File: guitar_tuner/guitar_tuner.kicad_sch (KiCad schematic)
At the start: 8 parts, among them SW1 Reset, SW2 Boot, U1 ESP32-S2-SOLO

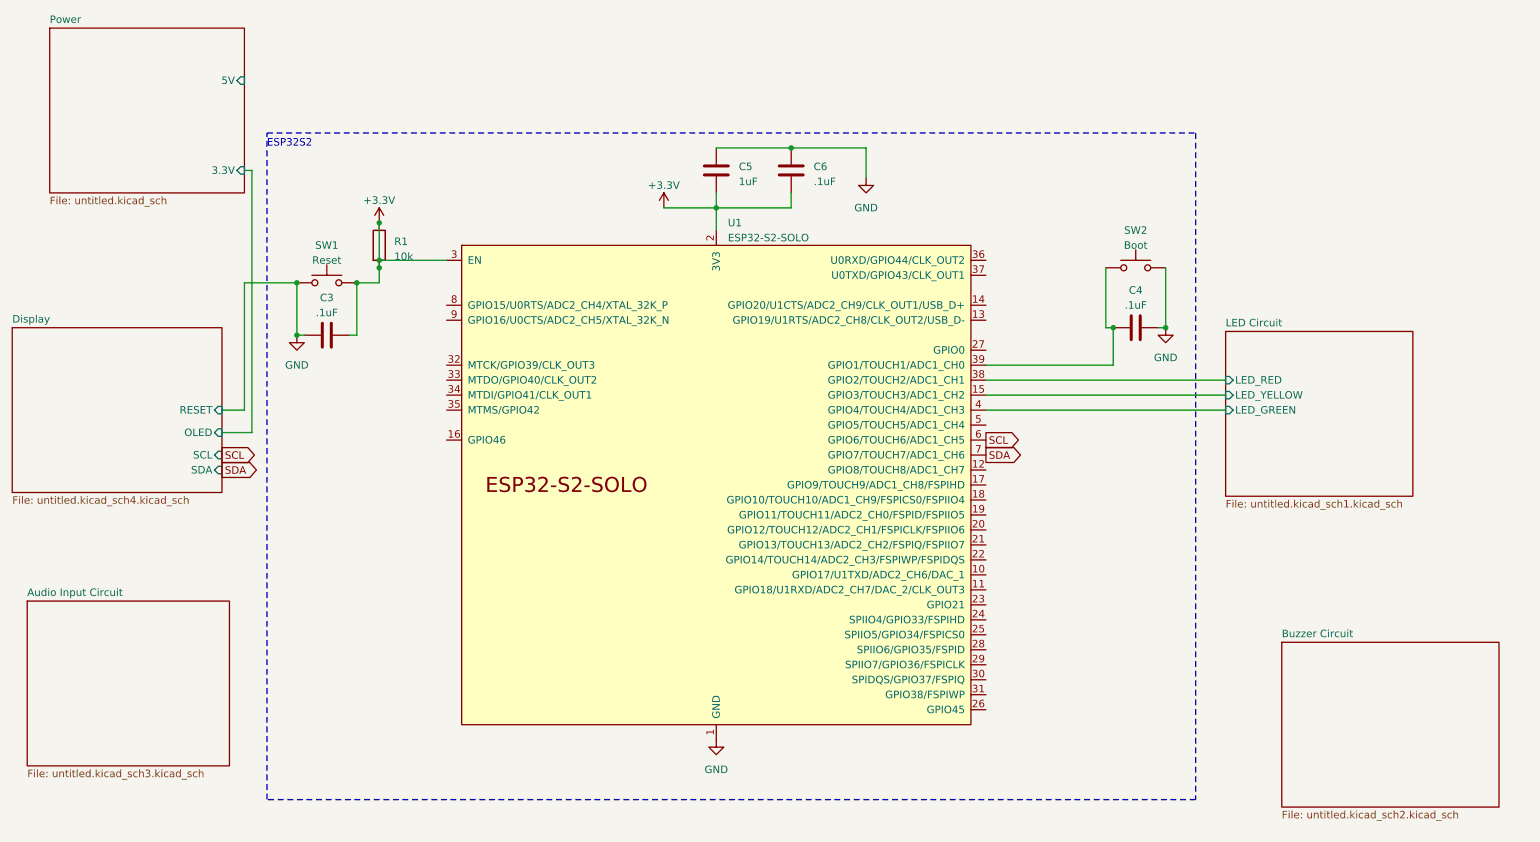
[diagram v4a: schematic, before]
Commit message: Connected power to buzzer and audio input circuits, made connections to microcontroller.
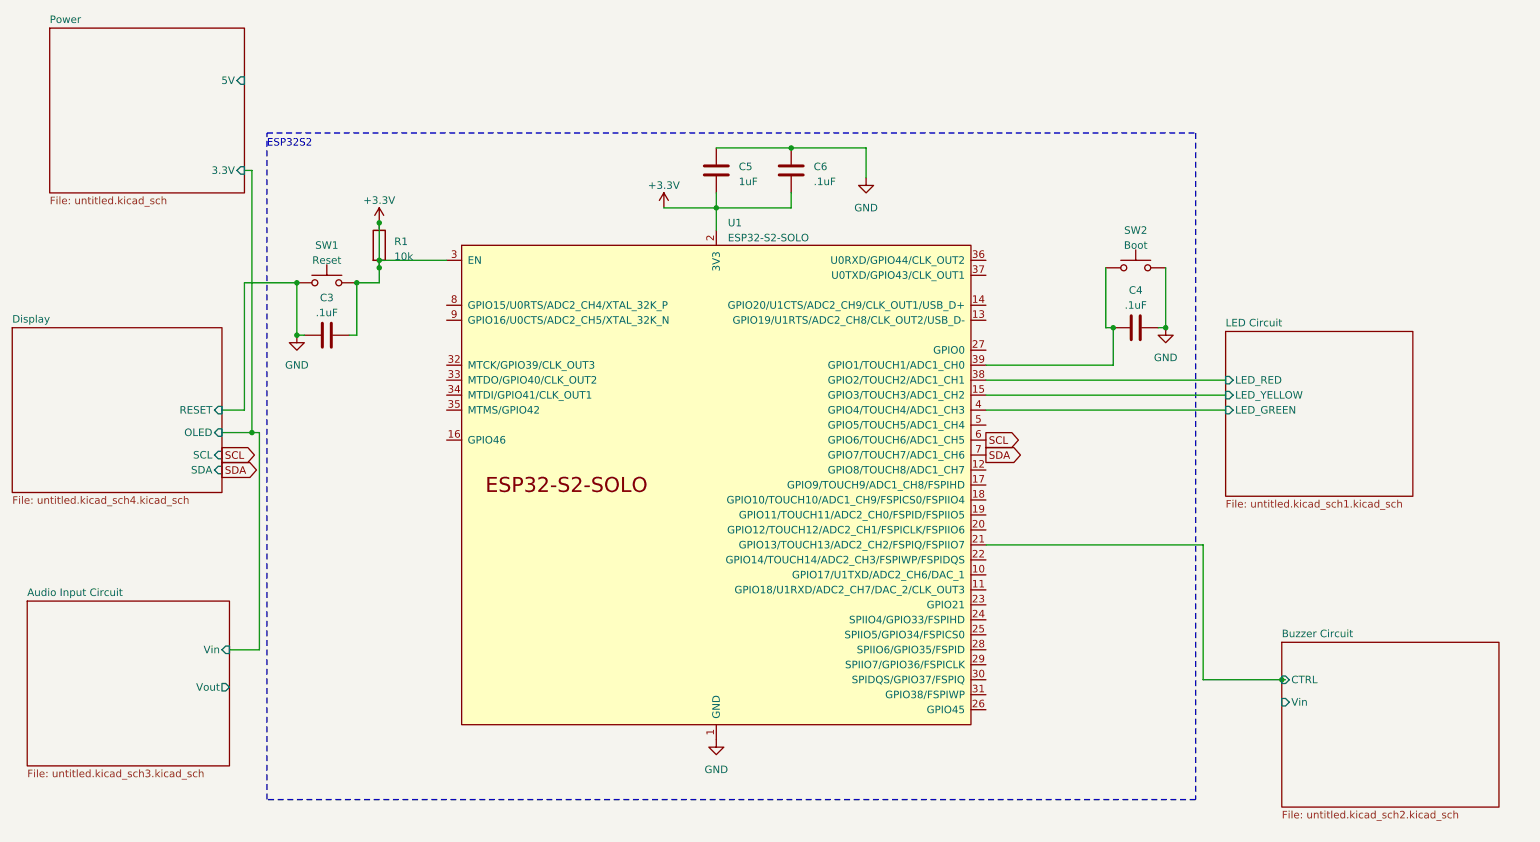
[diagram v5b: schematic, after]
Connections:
- net Buzzer Circuit/CTRL: now reaches U1.21 (GPIO13/TOUCH13/ADC2_CH2/FSPIQ/FSPIIO7)
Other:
- sheet Audio Input Circuit ports: added Vin, Vout; removed none
- sheet Buzzer Circuit ports: added CTRL, Vin; removed none
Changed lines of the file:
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@@
+	)
+	(junction
+		(at 58.42 91.44)
+		(diameter 0)
+		(color 0 0 0 0)
 	)
 	(junction
@@
 	)
 	(junction
+		(at 233.045 133.35)
+		(diameter 0)
+		(color 0 0 0 0)
+	)
+	(junction
 		(at 213.36 73.66)
 		(diameter 0)
@@
 	(wire
 		(pts
+			(xy 219.71 133.35) (xy 219.71 110.49)
+		)
+		(stroke
+			(width 0)
+			(type default)
+		)
+	)
+	(wire
+		(pts
 			(xy 74.93 74.93) (xy 76.2 74.93)
 		)
@@
 	(wire
 		(pts
+			(xy 59.69 128.27) (xy 54.61 128.27)
+		)
+		(stroke
+			(width 0)
+			(type default)
+		)
+	)
+	(wire
+		(pts
 			(xy 149.86 43.18) (xy 162.56 43.18)
 		)
@@
 	(wire
 		(pts
+			(xy 58.42 91.44) (xy 59.69 91.44)
+		)
+		(stroke
+			(width 0)
+			(type default)
+		)
+	)
+	(wire
+		(pts
 			(xy 80.01 55.88) (xy 80.01 62.23)
 		)
@@
 	(wire
 		(pts
+			(xy 233.045 133.35) (xy 219.71 133.35)
+		)
+		(stroke
+			(width 0)
+			(type default)
+		)
+	)
+	(wire
+		(pts
 			(xy 66.04 74.93) (xy 66.04 66.04)
 		)
@@
 	(wire
 		(pts
+			(xy 59.69 91.44) (xy 59.69 128.27)
+		)
+		(stroke
+			(width 0)
+			(type default)
+		)
+	)
+	(wire
+		(pts
 			(xy 137.16 53.34) (xy 137.16 57.15)
 		)
@@
 	(wire
 		(pts
+			(xy 233.68 133.35) (xy 233.045 133.35)
+		)
+		(stroke
+			(width 0)
+			(type default)
+		)
+	)
+	(wire
+		(pts
 			(xy 203.2 63.5) (xy 203.2 73.66)
 		)
@@
 		(pts
 			(xy 80.01 66.04) (xy 76.2 66.04)
+		)
+		(stroke
+			(width 0)
+			(type default)
+		)
+	)
+	(wire
+		(pts
+			(xy 219.71 110.49) (xy 182.88 110.49)
 		)
 		(stroke
@@
 				(justify left)
 				(hide yes)
+			)
+		)
+	)
+	(netclass_flag ""
+		(length 2.54)
+		(shape round)
+		(at 54.61 134.62 270)
+		(fields_autoplaced yes)
+		(effects
+			(font
+				(size 1.27 1.27)
+			)
+			(justify right bottom)
+		)
+		(property "Netclass" "AUDIO"
+			(at 57.15 133.9215 90)
+			(effects
+				(font
+					(size 1.27 1.27)
+				)
+				(justify left)
+			)
+		)
+		(property "Component Class" ""
+			(at -45.72 -2.54 0)
+			(effects
+				(font
+					(size 1.27 1.27)
+					(italic yes)
+				)
+			)
+		)
+	)
+	(netclass_flag ""
+		(length 2.54)
+		(shape round)
+		(at 233.68 137.16 90)
+		(fields_autoplaced yes)
+		(effects
+			(font
+				(size 1.27 1.27)
+			)
+			(justify left bottom)
+		)
+		(property "Netclass" "5V"
+			(at 231.14 136.4615 90)
+			(effects
+				(font
+					(size 1.27 1.27)
+				)
+				(justify left)
+			)
+		)
+		(property "Component Class" ""
+			(at 3.81 -1.27 0)
+			(effects
+				(font
+					(size 1.27 1.27)
+					(italic yes)
+				)
+			)
+		)
+	)
+	(netclass_flag ""
+		(length 2.54)
+		(shape round)
+		(at 182.88 90.17 270)
+		(fields_autoplaced yes)
+		(effects
+			(font
+				(size 1.27 1.27)
+			)
+			(justify right bottom)
+		)
+		(property "Netclass" "AUDIO"
+			(at 185.42 89.4715 90)
+			(effects
+				(font
+					(size 1.27 1.27)
+				)
+				(justify left)
+			)
+		)
+		(property "Component Class" ""
+			(at 0 1.27 0)
+			(effects
+				(font
+					(size 1.27 1.27)
+					(italic yes)
+				)
+			)
+		)
+	)
+	(netclass_flag ""
+		(length 2.54)
+		(shape round)
+		(at 57.15 31.75 270)
+		(fields_autoplaced yes)
+		(effects
+			(font
+				(size 1.27 1.27)
+			)
+			(justify right bottom)
+		)
+		(property "Netclass" "5V"
+			(at 59.69 31.0515 90)
+			(effects
+				(font
+					(size 1.27 1.27)
+				)
+				(justify left)
+			)
+		)
+		(property "Component Class" ""
+			(at -71.12 -10.16 0)
+			(effects
+				(font
+					(size 1.27 1.27)
+					(italic yes)
+				)
 			)
 		)
@@
 			)
 		)
+		(pin "CTRL" input
+			(at 233.045 133.35 180)
+			(effects
+				(font
+					(size 1.27 1.27)
+				)
+				(justify left)
+			)
+		)
+		(pin "Vin" input
+			(at 233.045 137.16 180)
+			(effects
+				(font
+					(size 1.27 1.27)
+				)
+				(justify left)
+			)
+		)
 		(instances
 			(project "guitar_tuner"
@@
 			)
 		)
+		(pin "Vin" input
+			(at 54.61 128.27 0)
+			(effects
+				(font
+					(size 1.27 1.27)
+				)
+				(justify right)
+			)
+		)
+		(pin "Vout" output
+			(at 54.61 134.62 0)
+			(effects
+				(font
+					(size 1.27 1.27)
+				)
+				(justify right)
+			)
+		)

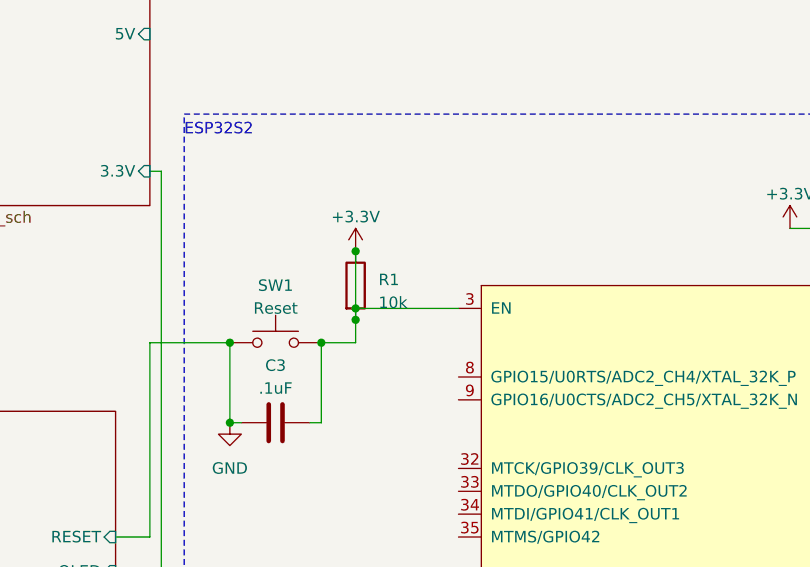
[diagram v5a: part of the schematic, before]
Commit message: Fixed short short with R1 and space out schematic for audio input.
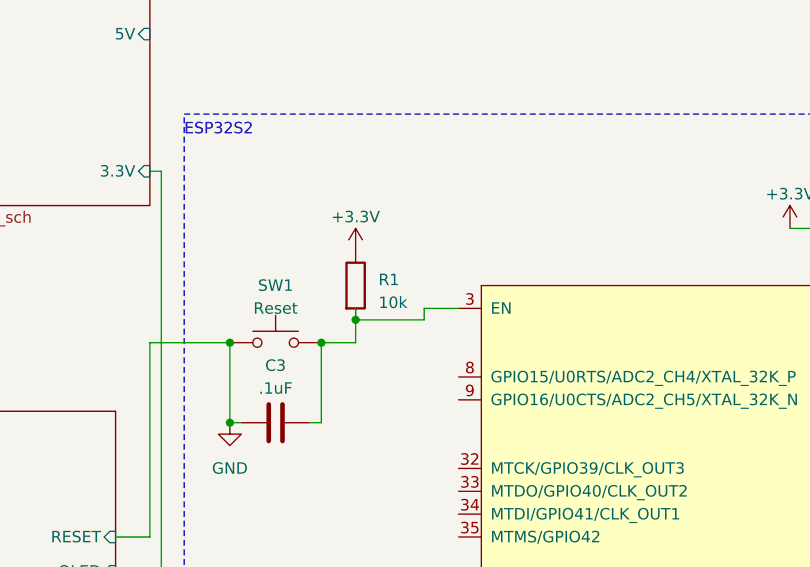
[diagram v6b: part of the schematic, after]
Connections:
- net +3.3V: no longer C3.2, R1.2, SW1.2, U1.3 (EN)
- new net: C3.2, R1.2, SW1.2, U1.3 (EN)
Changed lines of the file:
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@@
-	)
-	(junction
-		(at 80.01 62.23)
-		(diameter 0)
-		(color 0 0 0 0)
 	)
 	(junction
@@
 	)
 	(junction
-		(at 80.01 55.88)
-		(diameter 0)
-		(color 0 0 0 0)
-	)
-	(junction
 		(at 204.47 73.66)
 		(diameter 0)
@@
 	(wire
 		(pts
-			(xy 80.01 55.88) (xy 80.01 62.23)
-		)
-		(stroke
-			(width 0)
-			(type default)
-		)
-	)
-	(wire
-		(pts
 			(xy 57.15 66.04) (xy 66.04 66.04)
 		)
@@
 	(wire
 		(pts
+			(xy 87.63 63.5) (xy 87.63 62.23)
+		)
+		(stroke
+			(width 0)
+			(type default)
+		)
+	)
+	(wire
+		(pts
 			(xy 233.045 133.35) (xy 219.71 133.35)
 		)
@@
 	(wire
 		(pts
-			(xy 80.01 62.23) (xy 91.44 62.23)
-		)
-		(stroke
-			(width 0)
-			(type default)
-		)
-	)
-	(wire
-		(pts
 			(xy 58.42 46.99) (xy 57.15 46.99)
 		)
@@
 	(wire
 		(pts
+			(xy 87.63 62.23) (xy 91.44 62.23)
+		)
+		(stroke
+			(width 0)
+			(type default)
+		)
+	)
+	(wire
+		(pts
 			(xy 137.16 53.34) (xy 137.16 57.15)
 		)
@@
 		)
 		(stroke
+			(width 0)
+			(type default)
+		)
+	)
+	(wire
+		(pts
+			(xy 80.01 63.5) (xy 87.63 63.5)
+		)
+		(stroke

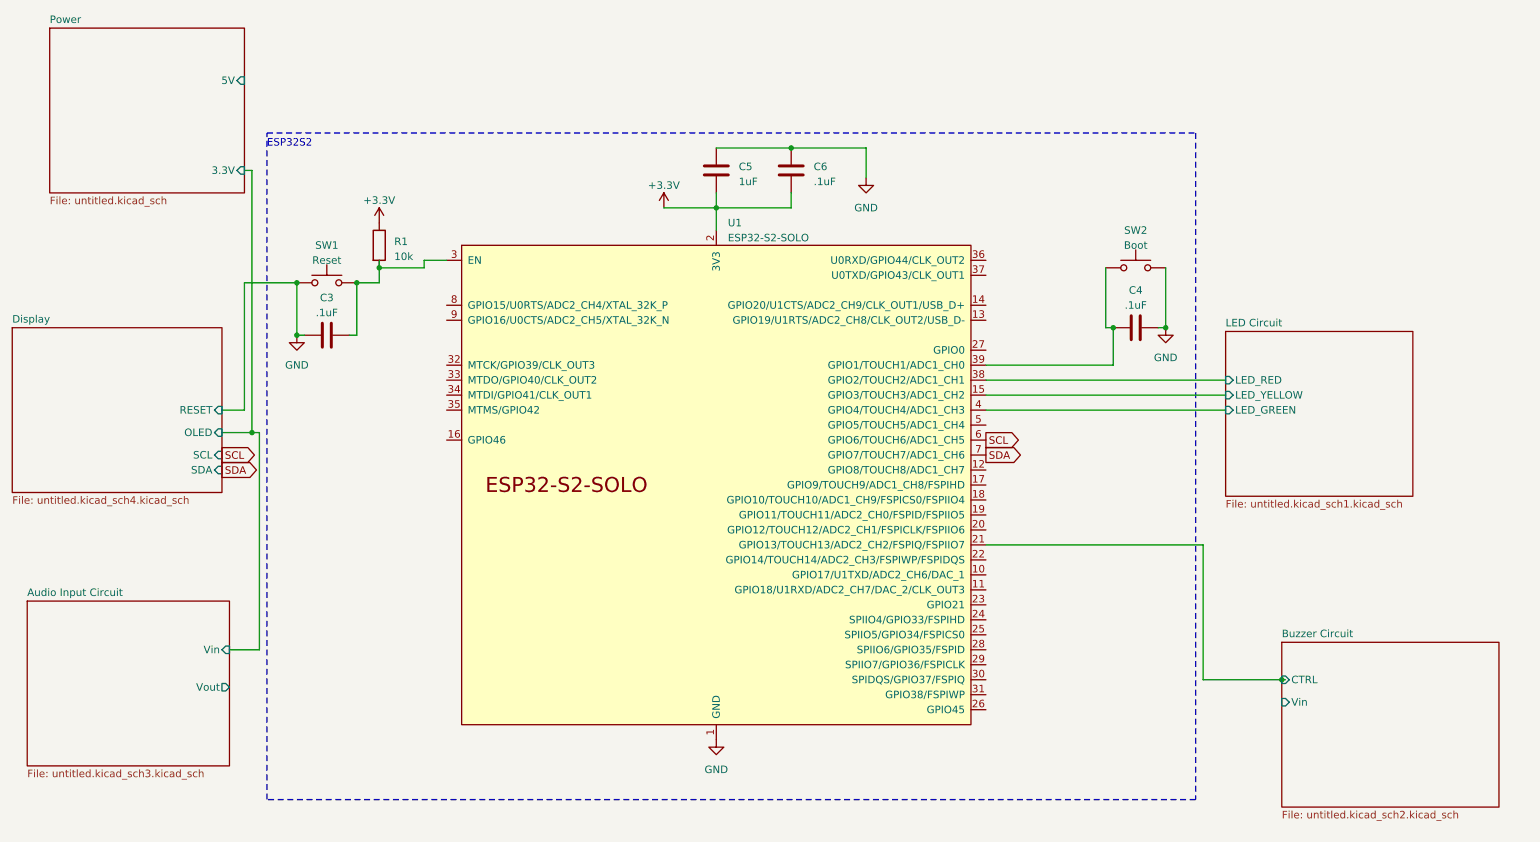
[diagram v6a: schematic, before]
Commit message: Multiple Schematic Fixes
- Created outputs from the power schematic for the D+ and D- pins and attached them to esp
- Changed net class directives to global labels as net class directives don't properly translate to layout (5V, Audio, 3.3V)
- Fixed buzzer schematic as the esp was not properly connected to it due to mismatched grid sizes
- Added power flags to voltage sources
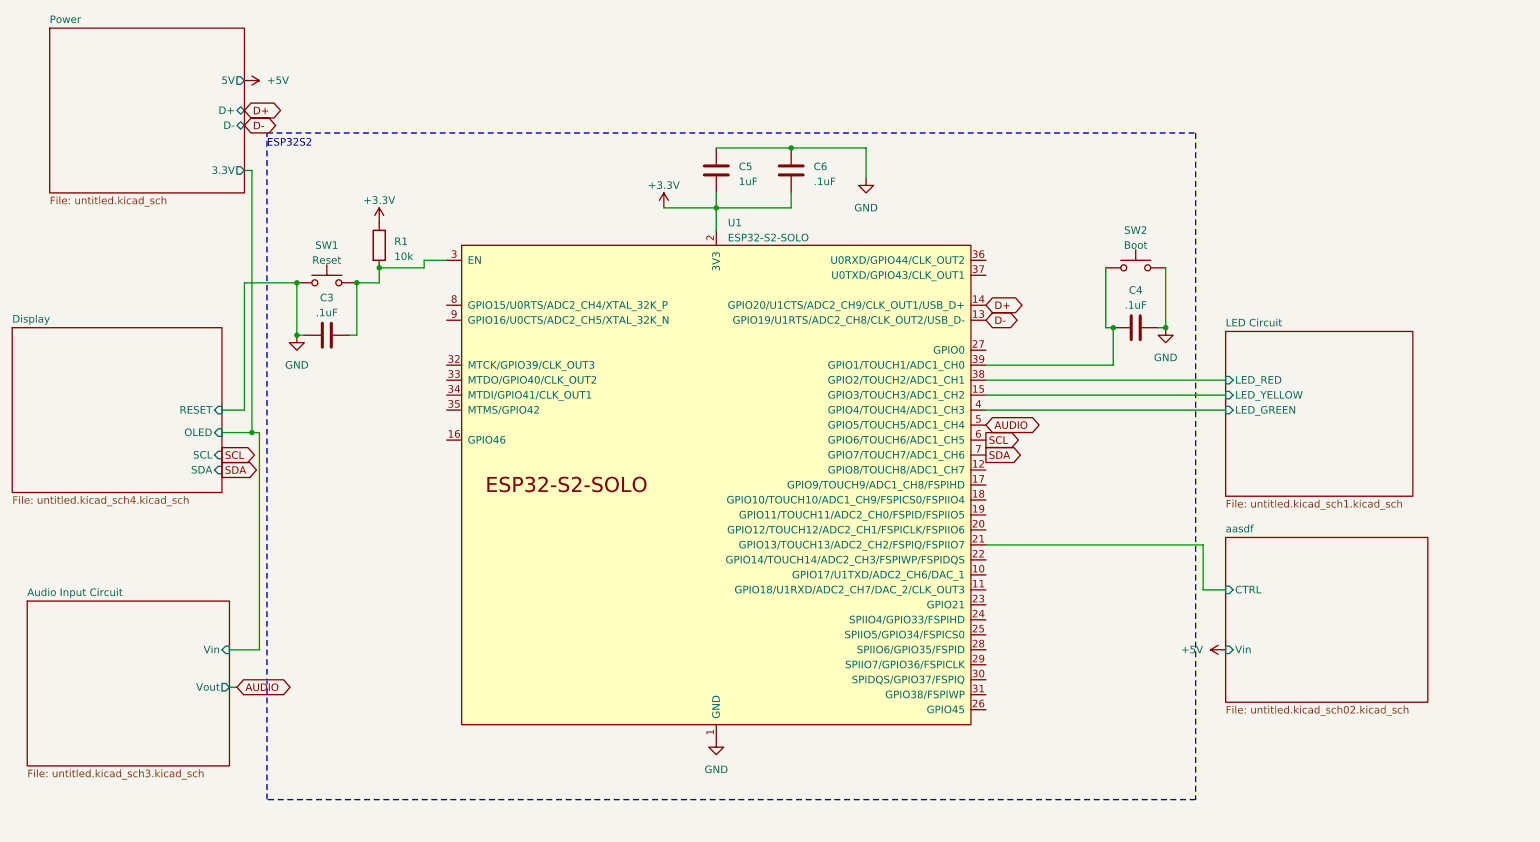
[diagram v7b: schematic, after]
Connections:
- net D-: now reaches U1.13 (GPIO19/U1RTS/ADC2_CH8/CLK_OUT2/USB_D-)
- net D+: now reaches U1.14 (GPIO20/U1CTS/ADC2_CH9/CLK_OUT1/USB_D+)
- net AUDIO: now reaches U1.5 (GPIO5/TOUCH5/ADC1_CH4)
- net Buzzer Circuit/CTRL renamed aasdf/CTRL
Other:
- removed sheet Buzzer Circuit
- added sheet aasdf (untitled.kicad_sch02.kicad_sch)
- sheet Power ports: added D+, D-; removed none
